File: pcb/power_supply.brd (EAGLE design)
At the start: 39.4 x 68.4 mm, 40 parts, among them P1 2k, Q1 DIODES_FMMT493ATADIODES_FMMT4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, Q2 DIODES_FMMT493ATADIODES_FMMT4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, Q3 DIODES_FMMT493ATADIODES_FMMT4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, Q4 DIODES_FMMT493ATADIODES_FMMT4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, Q5 DIODES_FMMT493ATADIODES_FMMT4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, Q6 DIODES_FMMT493ATADIODES_FMMT4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, Q7 DIODES_FMMT493ATADIODES_FMMT4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, Q8 DIODES_FMMT493ATADIODES_FMMT4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, U1 LM1085IT-ADJ, U2 LM1085IT-ADJ

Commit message: pcb - board partially updated
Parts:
- removed DC_CON: FC681478WURTH_694106301002, FC681478:WURTH_694106301002
- removed L2, L3, L4, L5, L6, L7, L8: (no value), con-phoenix-254:2POL254
- removed U2: LM1085IT-ADJ, LM1085IT-ADJ:TO254P1054X470X1955-3
- added C5, C6: 4.7u, rcl:C1206
- added C7, C8: 22u, rcl:C1206
- added CON1, CON2, CON3, CON4, CON5, CON6, CON7, CON8: +, con-phoenix-254:2POL254
- added D1: SSB44-E3_52T, SSB44-E3_52T:DIOM5436X244N
- added IC1: AP1507-D5-13, AP1507-D5-13:AP1507D513
- added R13, R15, R20: 4.3k, rcl:R0805
- added R14, R16: 22k, rcl:R0805
- added R17: 120, rcl:R0805
- added R18: 2.4k, rcl:R0805
- added R19: 3.3k, rcl:R0805
- C3, C4: value 10u -> 100n; device rcl:B/3528-21R -> rcl:C0603
- L1: value 1 -> HPI1040-220; device con-phoenix-254:2POL254 -> SRR1050A-151Y:INDM102100X510N
- R1, R3, R5, R7: value 100 -> 4.3k
- R10: value 120 -> 22k
- R11: value 330 -> 4.3k
- R12: value 39 -> 22k
- R2, R4, R6, R8: value 100 -> 22k
- R9: value 120 -> 4.3k
- moved ACC1 89.4 mm to (11.7, 7.61), turned to 0 degrees
- moved L1 88.8 mm to (15.2, 36.8), turned to 180 degrees
- moved ACC2 82.8 mm to (18.7, 7.61), turned to 0 degrees
- moved SWITCH 75.6 mm to (25.7, 7.61), turned to 0 degrees
- moved RASPBERRY 69.9 mm to (29.2, 44.5)
- moved Q8 63.8 mm to (22.9, 63.5), turned to 270 degrees
- moved R10 62.6 mm to (34.3, 49.5), turned to 90 degrees
- moved U1 58.3 mm to (44.5, 8.89)
- moved C1 58.1 mm to (38.8, 5.37)
- moved Q1 56.2 mm to (44.5, 26.7), turned to 270 degrees
- moved R12 55.5 mm to (33.0, 55.9)
- moved R1 55.3 mm to (39.4, 27.9)
- moved R7 55.1 mm to (39.4, 44.5)
- moved R5 55.0 mm to (39.4, 39.4)
- moved R3 55.0 mm to (39.4, 34.3)
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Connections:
- removed net 5V: C4.+, R10.2, RASPBERRY.2, RASPBERRY.4, U2.2
- removed net N$11: Q5.1, R5.2
- removed net N$12: L5.1, Q5.3
- removed net N$15: Q7.1, R7.2
- removed net N$16: L7.1, Q7.3
- removed net N$3 (its old number): ACC2.2, DC_CON.P$3
- removed net N$30: R11.1, R12.2
- removed net N$31: ACC1.1, DC_CON.P$1, SWITCH.2
- removed net N$8: L3.1, Q3.3
- new net N$32: D1.1, IC1.2, L1.1
- new net N$33: Q6.1, R11.2
- new net N$34: CON6.1, Q6.3
- new net N$37: Q7.1, R13.2
- new net N$38: CON7.1, Q7.3
- new net N$4: IC1.4, R18.2, R19.2
- new net N$41: Q8.1, R15.2
- new net N$42: CON8.1, Q8.3
- new net RASP_SUPPLY: C7.1, C8.1, L1.2, R20.1, RASPBERRY.2, RASPBERRY.4
- net BAT: now also C3.1, C4.1, C5.1, C6.1, IC1.1, SWITCH.2; no longer C3.+, SWITCH.1, U2.3
- net GND: now also ACC1.1, C3.2, C4.2, C5.2, C6.2, C7.2, C8.2, D1.2, IC1.3, IC1.5, IC1.6, R10.1, R14.1, R16.1, R18.1, R2.1, R4.1, R6.1, R8.1; no longer C3.-, C4.-, DC_CON.P$2
- net LIGHTS+: now also CON1.2, CON2.2, CON3.2, CON4.2, CON5.2, CON6.2, CON7.2, CON8.2, R17.2; no longer L1.2, L2.2, L3.2, L4.2, L5.2, L6.2, L7.2, L8.2, R9.2
- net N$1: now also CON1.1; no longer L1.1
- net N$10: now also CON3.1, Q3.3; no longer L4.1, Q4.3
- net N$13: now also Q4.1, R7.2; no longer Q6.1, R6.2
- net N$14: now also CON4.1, Q4.3; no longer L6.1, Q6.3
- net N$17: now also Q5.1, R9.2; no longer Q8.1, R8.2
- net N$18: now also CON5.1, Q5.3; no longer L8.1, Q8.3
- net N$19: now also R2.2
- net N$2: now also R19.1, R20.2; no longer R10.1, R11.2, U2.1
- net N$20: now also R3.1, R4.2; no longer R2.1
- net N$21: now also R5.1, R6.2; no longer R3.1
- net N$23: now also R7.1, R8.2; no longer R4.1
- net N$24: now also R10.2, R9.1; no longer R5.1
- net N$25: now also R11.1, R12.2; no longer R6.1
- net N$26: now also R13.1, R14.2; no longer R7.1
- net N$27: now also R15.1, R16.2; no longer R8.1
- net N$29: now also R17.1; no longer R9.1
- net N$5: now also R3.2; no longer R2.2
- net N$6: now also CON2.1; no longer L2.1
- net N$7: now also ACC2.2, SWITCH.1; no longer Q3.1, R3.2
- net N$9: now also Q3.1, R5.2; no longer Q4.1, R4.2
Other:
- board size 39.4 x 68.4 mm -> 57.3 x 66.4 mm
- board text removed: "+"

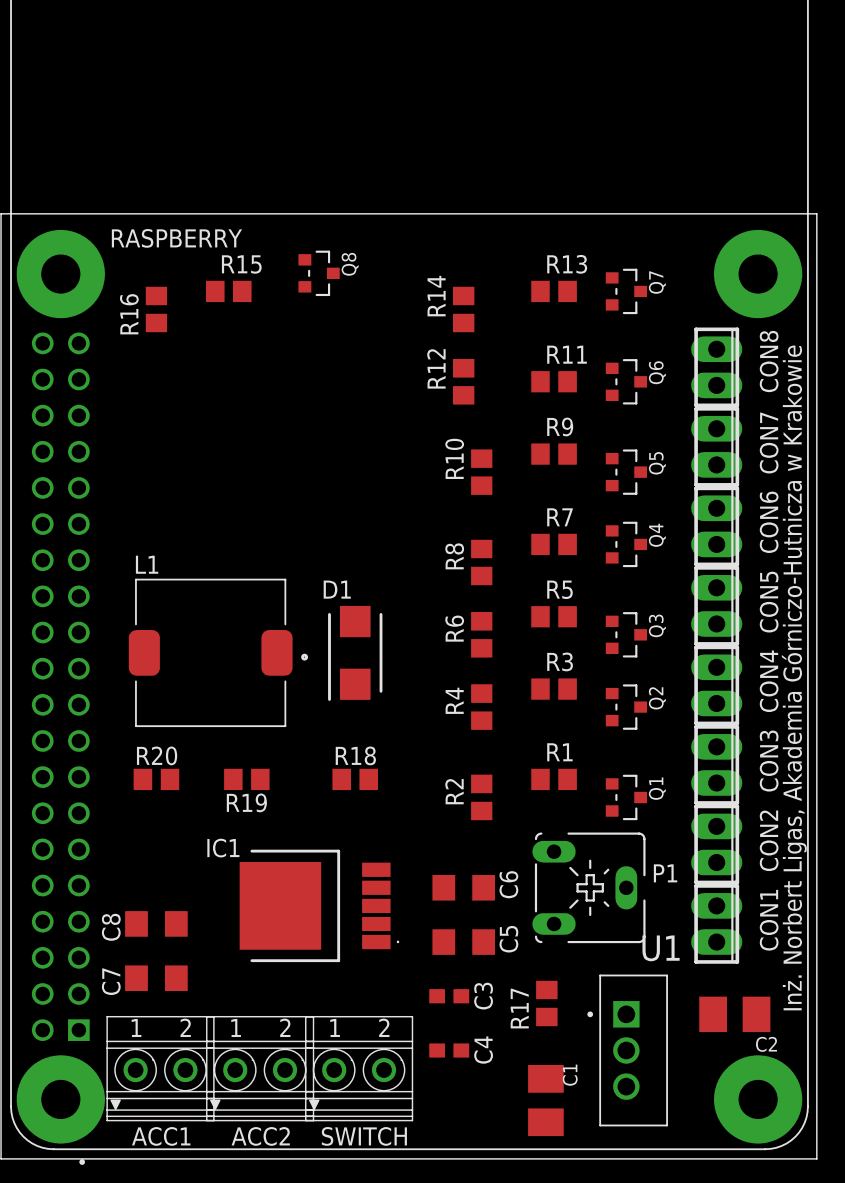
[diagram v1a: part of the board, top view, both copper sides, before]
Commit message: pcb - elements placed in the right places
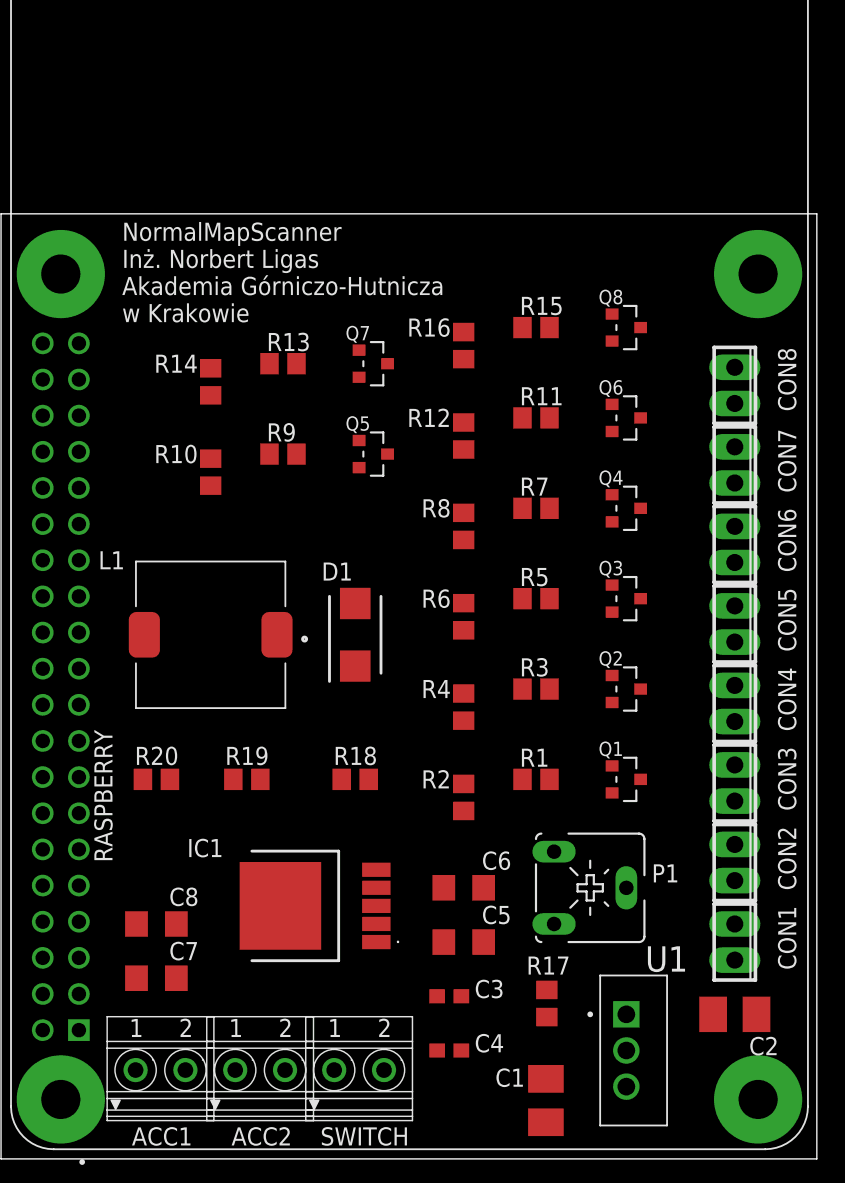
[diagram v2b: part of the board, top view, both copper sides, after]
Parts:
- moved Q8 21.9 mm to (44.5, 59.7)
- moved R16 21.7 mm to (33.0, 58.4)
- moved R15 21.7 mm to (38.1, 59.7)
- moved R13 19.7 mm to (20.3, 57.1)
- moved R10 19.0 mm to (15.2, 49.5)
- moved R9 19.0 mm to (20.3, 50.8)
- moved Q7 18.5 mm to (26.7, 57.1)
- moved R14 18.5 mm to (15.2, 55.9)
- moved Q5 17.8 mm to (26.7, 50.8)
- moved R12 3.81 mm to (33.0, 52.1)
- moved R11 2.84 mm to (38.1, 53.3)
- moved R7 2.84 mm to (38.1, 47.0)
- moved R8 2.84 mm to (33.0, 45.7)
- moved Q3 2.54 mm to (44.5, 40.6)
- moved Q4 2.54 mm to (44.5, 47.0)
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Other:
- board text added: "NormalMapScanner Inż. Norbert Ligas Akademia Górniczo-Hutnicza w Krakowie"
- board text removed: "Inż. Norbert Ligas, Akademia Górniczo-Hutnicza w Krakowie"

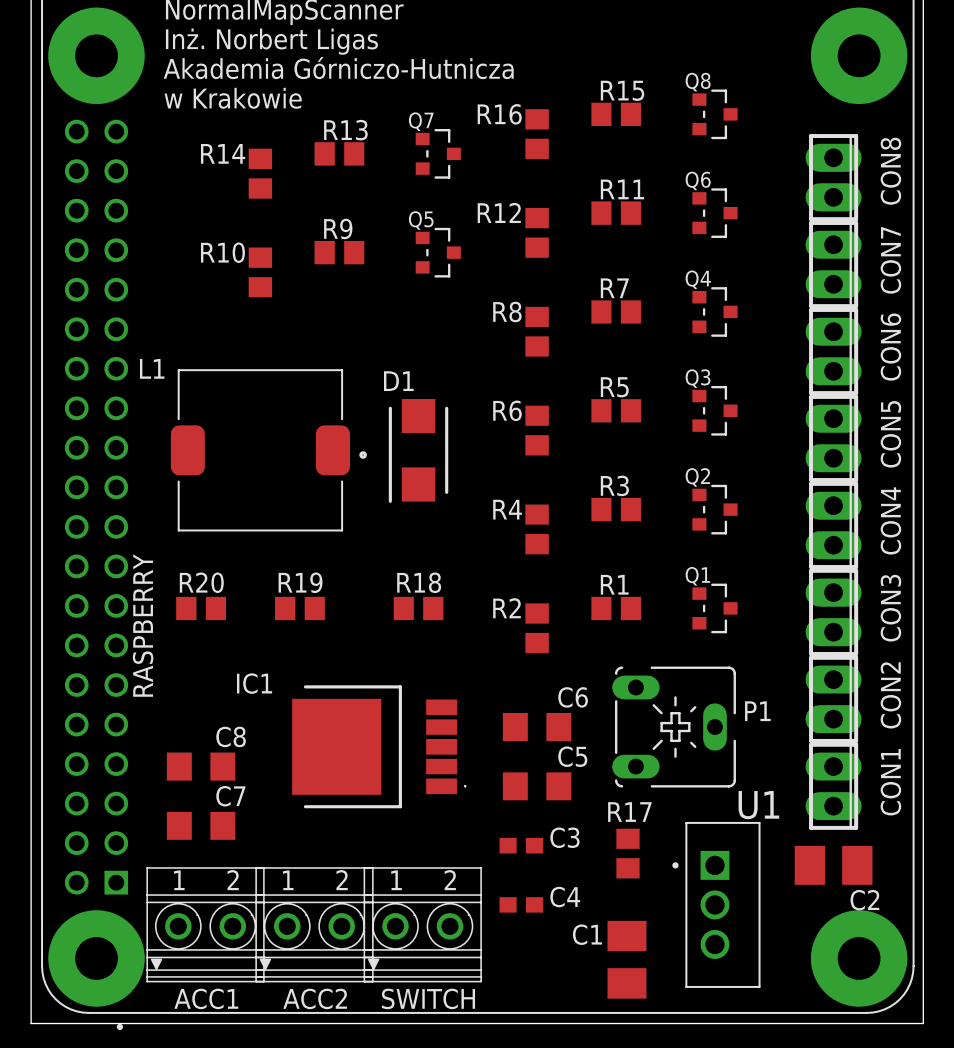
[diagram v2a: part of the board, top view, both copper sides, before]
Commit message: pcb - routes placed
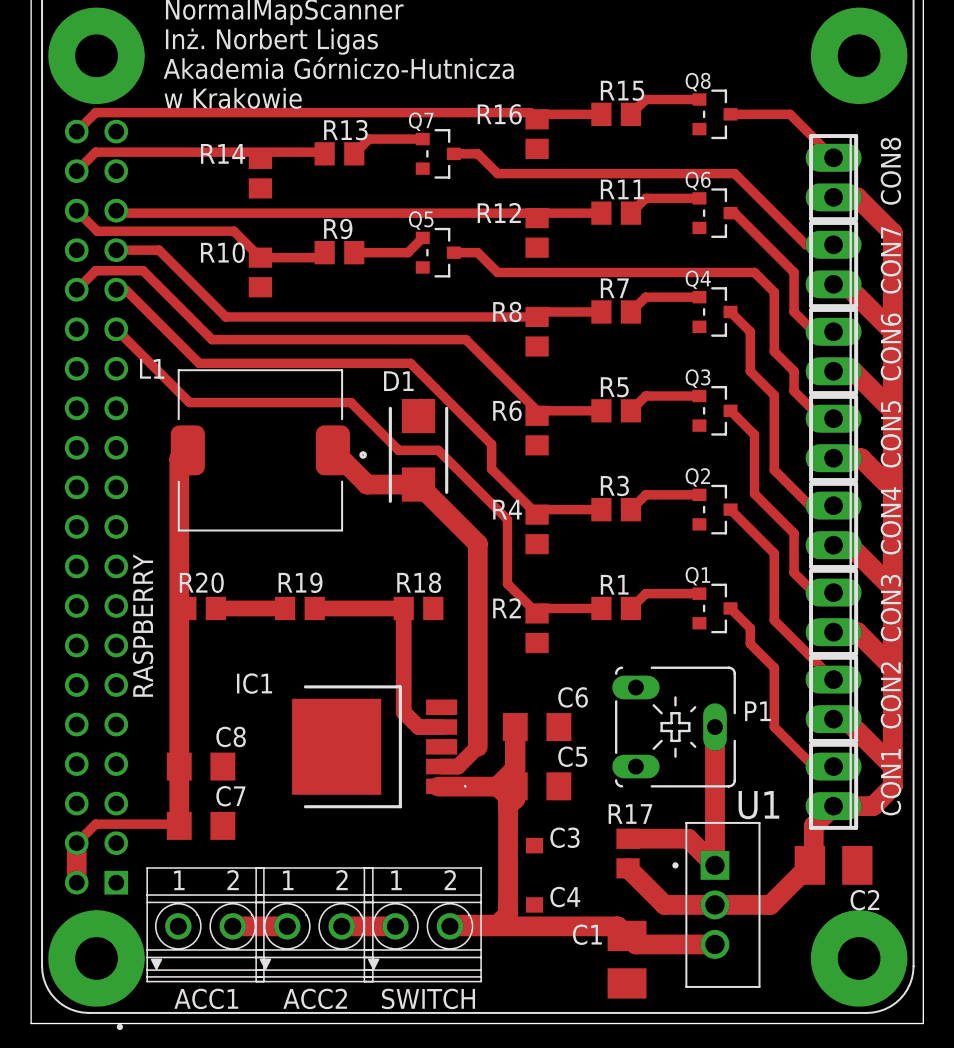
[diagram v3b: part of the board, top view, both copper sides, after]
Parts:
- turned R17 to 270 degrees
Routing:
- net LIGHTS+: track 0.00 -> 92.2 mm
- net BAT: track 0.00 -> 44.6 mm
- net N$19: track 0.00 -> 41.3 mm
- net N$21: track 0.00 -> 38.4 mm
- net N$20: track 0.00 -> 38.2 mm
- net N$27: track 0.00 -> 34.5 mm
- net RASP_SUPPLY: track 0.00 -> 34.5 mm
- net N$23: track 0.00 -> 33.1 mm
- net N$18: track 0.00 -> 31.8 mm
- net N$25: track 0.00 -> 31.2 mm
- net N$32: track 0.00 -> 27.7 mm
- net N$38: track 0.00 -> 26.8 mm
- net N$24: track 0.00 -> 17.3 mm
- net N$26: track 0.00 -> 16.9 mm
- net N$14: track 0.00 -> 16.1 mm
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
